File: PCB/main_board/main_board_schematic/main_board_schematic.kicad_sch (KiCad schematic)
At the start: 33 parts, among them J1 Conn_01x02, P1 USB_C_Plug_USB2.0, SW1 tactile_switch, SW2 SW_MEC_5G, U1 NCP1117-3.3_SOT223, U2 RP2040, U3 W25Q128JVS, Y1 12MHZ

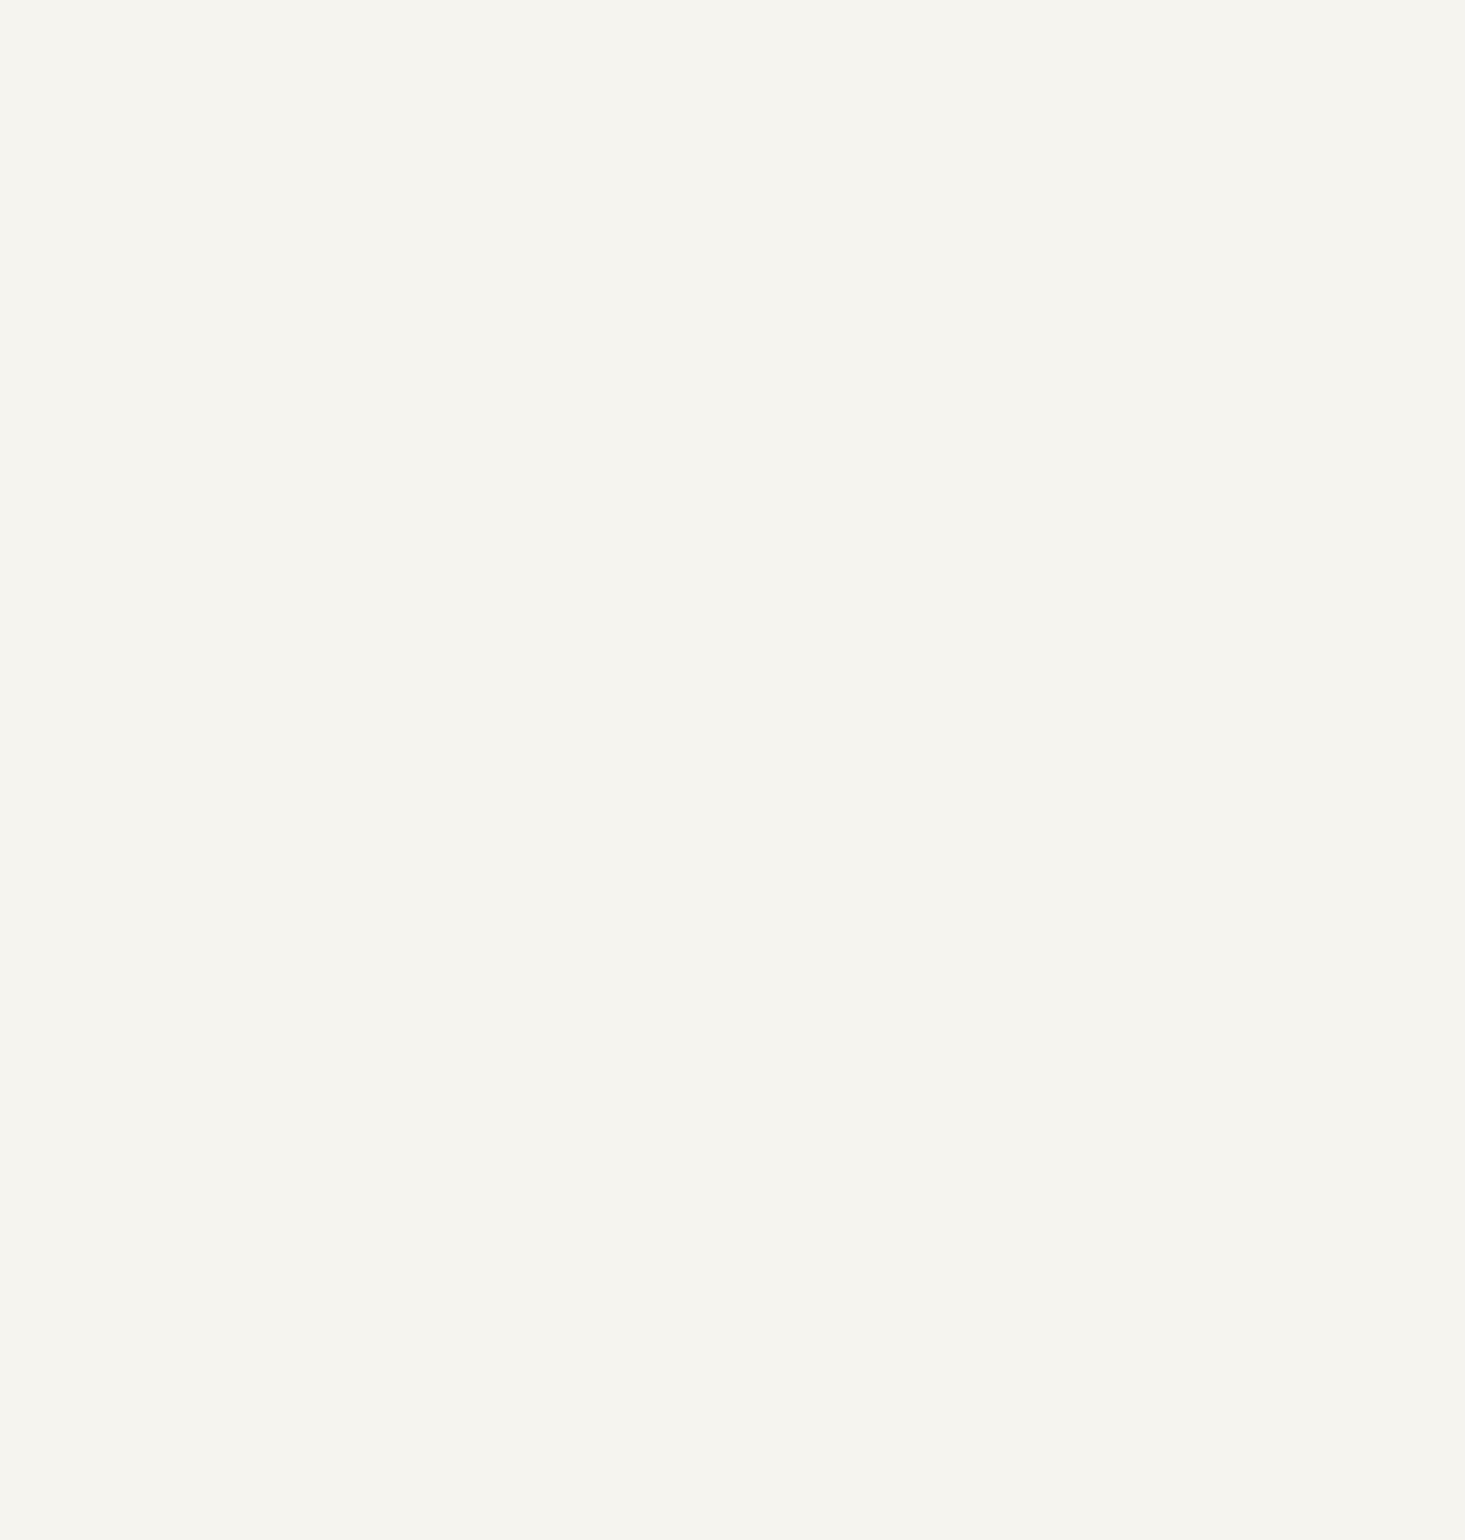
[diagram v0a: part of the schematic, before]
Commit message: Added all the siwtches to the board
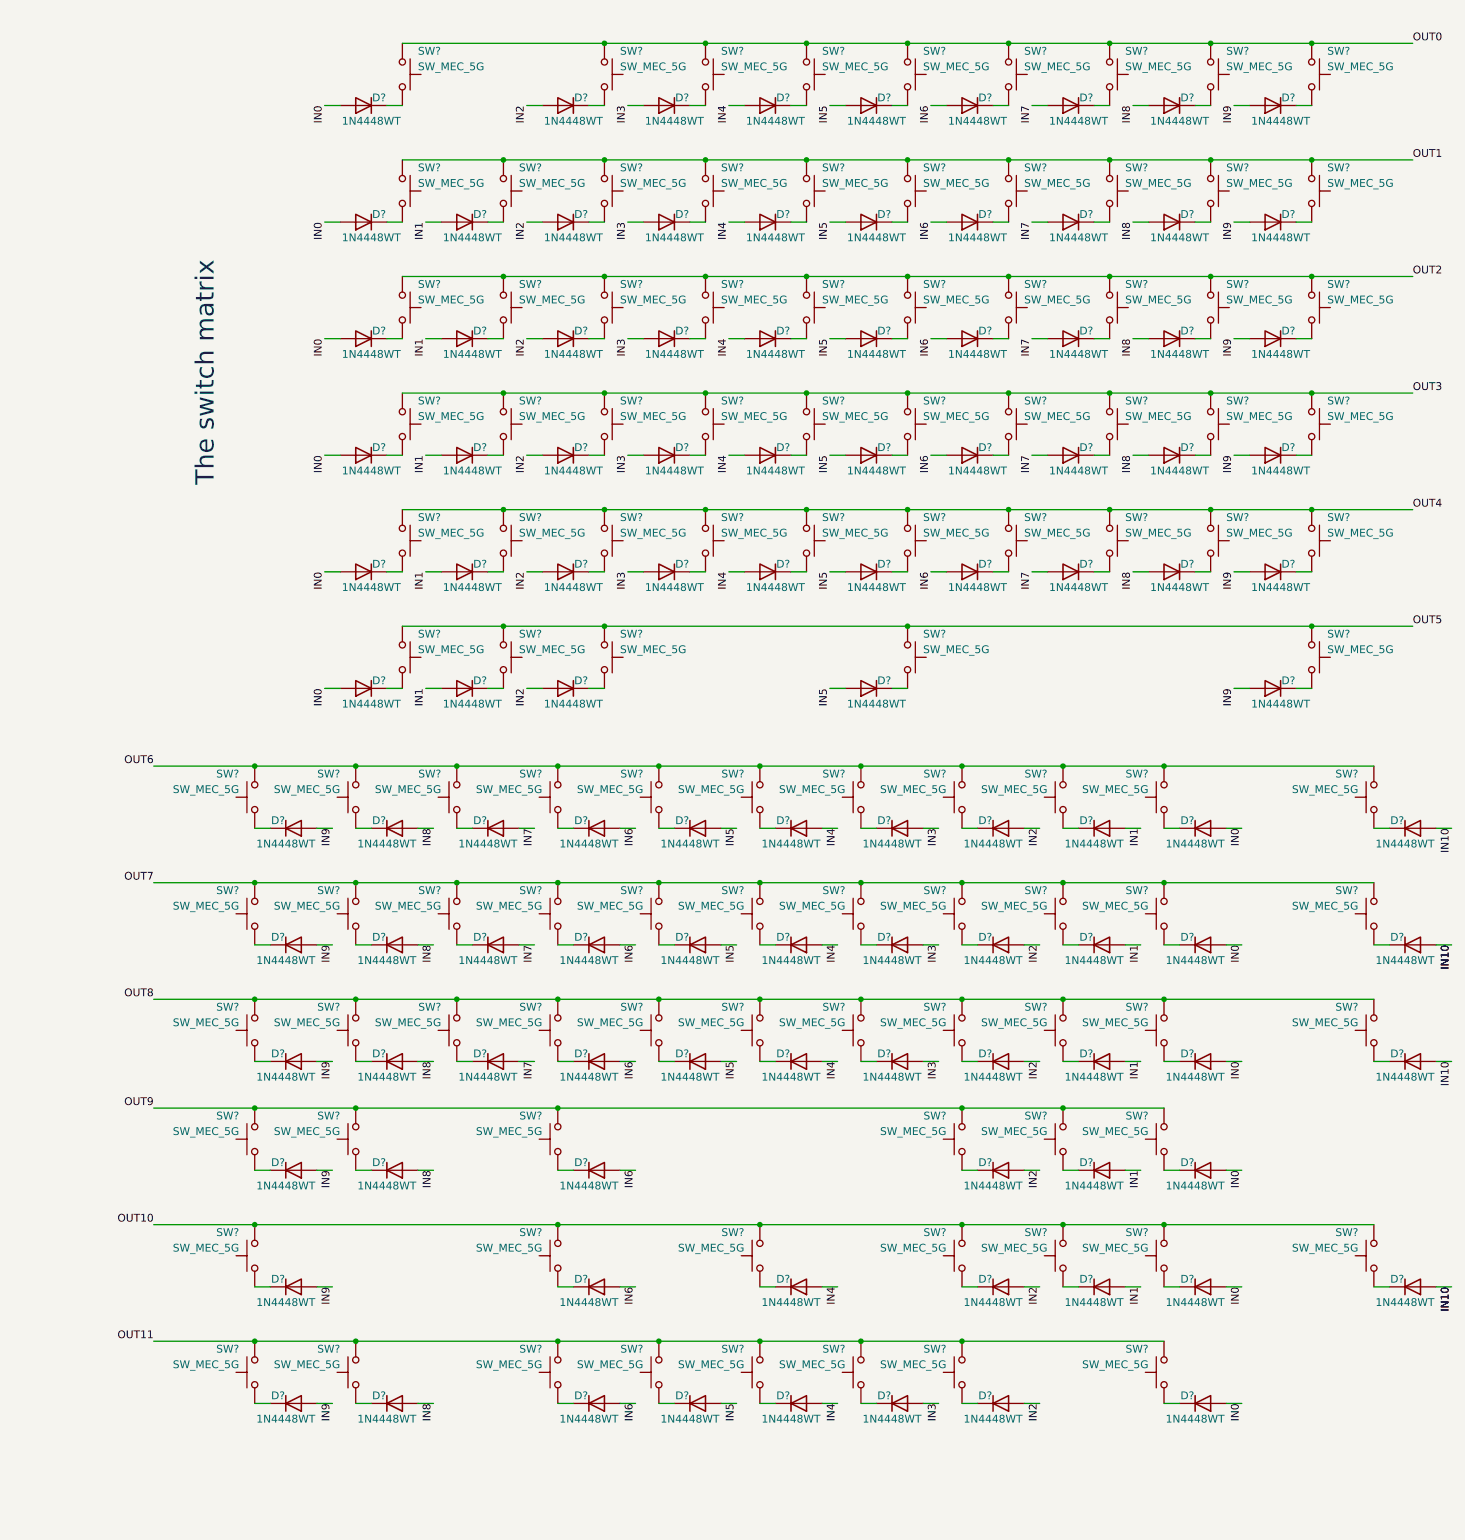
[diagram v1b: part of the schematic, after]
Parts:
- added D? (x108): 1N4448WT, Diode_SMD:D_SOD-523, symbol Diode:1N4448WT
- added SW? (x108): SW_MEC_5G, symbol Switch:SW_MEC_5G
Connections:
- new net: D?.1 (K), SW?.3 (B), SW?.4 (B) (x108)
- new net IN0: D?.2 (A), D?.2 (A), D?.2 (A), D?.2 (A), D?.2 (A), D?.2 (A), D?.2 (A), D?.2 (A), D?.2 (A), D?.2 (A), D?.2 (A), D?.2 (A)
- new net IN1: D?.2 (A), D?.2 (A), D?.2 (A), D?.2 (A), D?.2 (A), D?.2 (A), D?.2 (A), D?.2 (A), D?.2 (A), D?.2 (A)
- new net IN10: D?.2 (A), D?.2 (A), D?.2 (A), D?.2 (A)
- new net IN2: D?.2 (A), D?.2 (A), D?.2 (A), D?.2 (A), D?.2 (A), D?.2 (A), D?.2 (A), D?.2 (A), D?.2 (A), D?.2 (A), D?.2 (A), D?.2 (A)
- new net IN3: D?.2 (A), D?.2 (A), D?.2 (A), D?.2 (A), D?.2 (A), D?.2 (A), D?.2 (A), D?.2 (A), D?.2 (A)
- new net IN4: D?.2 (A), D?.2 (A), D?.2 (A), D?.2 (A), D?.2 (A), D?.2 (A), D?.2 (A), D?.2 (A), D?.2 (A), D?.2 (A)
- new net IN5: D?.2 (A), D?.2 (A), D?.2 (A), D?.2 (A), D?.2 (A), D?.2 (A), D?.2 (A), D?.2 (A), D?.2 (A), D?.2 (A)
- new net IN6: D?.2 (A), D?.2 (A), D?.2 (A), D?.2 (A), D?.2 (A), D?.2 (A), D?.2 (A), D?.2 (A), D?.2 (A), D?.2 (A), D?.2 (A)
- new net IN7: D?.2 (A), D?.2 (A), D?.2 (A), D?.2 (A), D?.2 (A), D?.2 (A), D?.2 (A), D?.2 (A)
- new net IN8: D?.2 (A), D?.2 (A), D?.2 (A), D?.2 (A), D?.2 (A), D?.2 (A), D?.2 (A), D?.2 (A), D?.2 (A), D?.2 (A)
- new net IN9: D?.2 (A), D?.2 (A), D?.2 (A), D?.2 (A), D?.2 (A), D?.2 (A), D?.2 (A), D?.2 (A), D?.2 (A), D?.2 (A), D?.2 (A), D?.2 (A)
- new net OUT0: SW?.1 (A), SW?.1 (A), SW?.1 (A), SW?.1 (A), SW?.1 (A), SW?.1 (A), SW?.1 (A), SW?.1 (A), SW?.1 (A), SW?.2 (A), SW?.2 (A), SW?.2 (A), SW?.2 (A), SW?.2 (A), SW?.2 (A), SW?.2 (A), SW?.2 (A), SW?.2 (A)
- new net OUT1: SW?.1 (A), SW?.1 (A), SW?.1 (A), SW?.1 (A), SW?.1 (A), SW?.1 (A), SW?.1 (A), SW?.1 (A), SW?.1 (A), SW?.1 (A), SW?.2 (A), SW?.2 (A), SW?.2 (A), SW?.2 (A), SW?.2 (A), SW?.2 (A), SW?.2 (A), SW?.2 (A), SW?.2 (A), SW?.2 (A)
- new net OUT10: SW?.1 (A), SW?.1 (A), SW?.1 (A), SW?.1 (A), SW?.1 (A), SW?.1 (A), SW?.1 (A), SW?.2 (A), SW?.2 (A), SW?.2 (A), SW?.2 (A), SW?.2 (A), SW?.2 (A), SW?.2 (A)
- new net OUT11: SW?.1 (A), SW?.1 (A), SW?.1 (A), SW?.1 (A), SW?.1 (A), SW?.1 (A), SW?.1 (A), SW?.1 (A), SW?.2 (A), SW?.2 (A), SW?.2 (A), SW?.2 (A), SW?.2 (A), SW?.2 (A), SW?.2 (A), SW?.2 (A)
- new net OUT2: SW?.1 (A), SW?.1 (A), SW?.1 (A), SW?.1 (A), SW?.1 (A), SW?.1 (A), SW?.1 (A), SW?.1 (A), SW?.1 (A), SW?.1 (A), SW?.2 (A), SW?.2 (A), SW?.2 (A), SW?.2 (A), SW?.2 (A), SW?.2 (A), SW?.2 (A), SW?.2 (A), SW?.2 (A), SW?.2 (A)
- new net OUT3: SW?.1 (A), SW?.1 (A), SW?.1 (A), SW?.1 (A), SW?.1 (A), SW?.1 (A), SW?.1 (A), SW?.1 (A), SW?.1 (A), SW?.1 (A), SW?.2 (A), SW?.2 (A), SW?.2 (A), SW?.2 (A), SW?.2 (A), SW?.2 (A), SW?.2 (A), SW?.2 (A), SW?.2 (A), SW?.2 (A)
- new net OUT4: SW?.1 (A), SW?.1 (A), SW?.1 (A), SW?.1 (A), SW?.1 (A), SW?.1 (A), SW?.1 (A), SW?.1 (A), SW?.1 (A), SW?.1 (A), SW?.2 (A), SW?.2 (A), SW?.2 (A), SW?.2 (A), SW?.2 (A), SW?.2 (A), SW?.2 (A), SW?.2 (A), SW?.2 (A), SW?.2 (A)
- new net OUT5: SW?.1 (A), SW?.1 (A), SW?.1 (A), SW?.1 (A), SW?.1 (A), SW?.2 (A), SW?.2 (A), SW?.2 (A), SW?.2 (A), SW?.2 (A)
- new net OUT6: SW?.1 (A), SW?.1 (A), SW?.1 (A), SW?.1 (A), SW?.1 (A), SW?.1 (A), SW?.1 (A), SW?.1 (A), SW?.1 (A), SW?.1 (A), SW?.1 (A), SW?.2 (A), SW?.2 (A), SW?.2 (A), SW?.2 (A), SW?.2 (A), SW?.2 (A), SW?.2 (A), SW?.2 (A), SW?.2 (A), SW?.2 (A), SW?.2 (A)
- new net OUT7: SW?.1 (A), SW?.1 (A), SW?.1 (A), SW?.1 (A), SW?.1 (A), SW?.1 (A), SW?.1 (A), SW?.1 (A), SW?.1 (A), SW?.1 (A), SW?.1 (A), SW?.2 (A), SW?.2 (A), SW?.2 (A), SW?.2 (A), SW?.2 (A), SW?.2 (A), SW?.2 (A), SW?.2 (A), SW?.2 (A), SW?.2 (A), SW?.2 (A)
- new net OUT8: SW?.1 (A), SW?.1 (A), SW?.1 (A), SW?.1 (A), SW?.1 (A), SW?.1 (A), SW?.1 (A), SW?.1 (A), SW?.1 (A), SW?.1 (A), SW?.1 (A), SW?.2 (A), SW?.2 (A), SW?.2 (A), SW?.2 (A), SW?.2 (A), SW?.2 (A), SW?.2 (A), SW?.2 (A), SW?.2 (A), SW?.2 (A), SW?.2 (A)
- new net OUT9: SW?.1 (A), SW?.1 (A), SW?.1 (A), SW?.1 (A), SW?.1 (A), SW?.1 (A), SW?.2 (A), SW?.2 (A), SW?.2 (A), SW?.2 (A), SW?.2 (A), SW?.2 (A)
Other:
- note added: "The switch matrix"

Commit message: Moved to kicad7 and added key stabilizers
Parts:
- added S1, S2, S3, S4, S5, S6, S7, S8: MX_stab, PCM_marbastlib-mx:STAB_MX_P_6.25u, symbol PCM_marbastlib-mx:MX_stab
- gave numbers to parts that had none: 216
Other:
- note added: "Key stabilizers"
- moved on the sheet: D1, D10, D100, D101, D102, D103, D104, D105, D106, D107, D108, D11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
